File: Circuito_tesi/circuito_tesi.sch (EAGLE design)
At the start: 35 parts, among them IC3.3 317T, IC5 317T, U1 NRF52832, U2 BME688, U3 MICS-6814, U4 OPA2277PA, U5 OPA2277PA

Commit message: Aggiunti circuiti su board
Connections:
- net 3.3: no longer B1.GND, B1.GND@2
- net GND: now also B1.GND, B1.GND@2
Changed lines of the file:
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@@
 <net name="3.3" class="0">
-<segment>
-<pinref part="B1" gate="G$1" pin="GND"/>
-<wire x1="-129.54" y1="190.5" x2="-109.22" y2="190.5" width="0.1524" layer="91"/>
-<wire x1="-109.22" y1="190.5" x2="-109.22" y2="195.58" width="0.1524" layer="91"/>
-<pinref part="GND5" gate="1" pin="GND"/>
-<wire x1="-109.22" y1="195.58" x2="-104.14" y2="195.58" width="0.1524" layer="91"/>
-</segment>
-<segment>
-<pinref part="B1" gate="G$1" pin="GND@2"/>
-<wire x1="-162.56" y1="190.5" x2="-180.34" y2="190.5" width="0.1524" layer="91"/>
-<wire x1="-180.34" y1="190.5" x2="-180.34" y2="195.58" width="0.1524" layer="91"/>
-<pinref part="GND6" gate="1" pin="GND"/>
-<wire x1="-180.34" y1="195.58" x2="-187.96" y2="195.58" width="0.1524" layer="91"/>
-</segment>
 <segment>
 <wire x1="-228.6" y1="104.14" x2="-228.6" y2="119.38" width="0.1524" layer="91"/>
@@
 <pinref part="820OHM" gate="G$1" pin="2"/>
 <pinref part="U4" gate="A" pin="V+"/>
-<pinref part="U4" gate="A" pin="V+"/>
 <junction x="93.98" y="195.58"/>
 <pinref part="U5" gate="A" pin="V+"/>
@@
 <wire x1="127" y1="104.14" x2="127" y2="101.6" width="0.1524" layer="91"/>
 </segment>
+<segment>
+<pinref part="B1" gate="G$1" pin="GND@2"/>
+<wire x1="-162.56" y1="190.5" x2="-180.34" y2="190.5" width="0.1524" layer="91"/>
+<wire x1="-180.34" y1="190.5" x2="-180.34" y2="195.58" width="0.1524" layer="91"/>
+<pinref part="GND6" gate="1" pin="GND"/>
+<wire x1="-180.34" y1="195.58" x2="-187.96" y2="195.58" width="0.1524" layer="91"/>
+</segment>
+<segment>
+<pinref part="B1" gate="G$1" pin="GND"/>
+<wire x1="-129.54" y1="190.5" x2="-109.22" y2="190.5" width="0.1524" layer="91"/>
+<wire x1="-109.22" y1="190.5" x2="-109.22" y2="195.58" width="0.1524" layer="91"/>
+<pinref part="GND5" gate="1" pin="GND"/>
+<wire x1="-109.22" y1="195.58" x2="-104.14" y2="195.58" width="0.1524" layer="91"/>
+</segment>
 </net>
 <net name="N$2" class="0">
@@
 <pinref part="BT2" gate="G$1" pin="+"/>
 <wire x1="-109.22" y1="314.96" x2="-101.6" y2="314.96" width="0.1524" layer="91"/>
-</segment>
-</net>
-<net name="N$4" class="0">
-<segment>
-<pinref part="BT2" gate="G$1" pin="-"/>
-<pinref part="BT3" gate="G$1" pin="+"/>
-<wire x1="-86.36" y1="314.96" x2="-81.28" y2="314.96" width="0.1524" layer="91"/>
 </segment>
 </net>
@@
 </segment>
 </net>
+<net name="N$4" class="0">
+<segment>
+<pinref part="BT2" gate="G$1" pin="-"/>
+<pinref part="BT3" gate="G$1" pin="+"/>
+<wire x1="-86.36" y1="314.96" x2="-81.28" y2="314.96" width="0.1524" layer="91"/>
+</segment>
+</net>

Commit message: Aggiunte resistenze e condensatori smd
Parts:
- removed 10_MOHM, 10_MOHM1, 10_MOHM2, 130OHM, 27OHM, 300_OHM, 5_MOHM, 5_MOHM1, 5_MOHM2, 820OHM: 1614992-1, 1614992-1:1614992-1
- added R10: RMCF0603FT270R, Res_270OHM:RMCF0603FT270R
- added R11: RMCF0603FT130R, Res_130OHM:RMCF0603FT130R
- added R12: RMCF0603FT300R, Res_300OHM:RMCF0603FT300R
- added R3, R4, R5: RMCF0603FT10M0, Res_10MOHM_2:RMCF0603FT10M0
- added R6, R7, R8: RMCF0603FT5M10, Res_5.1MOHM:RMCF0603FT5M10
- added R9: RNCF0603DTE820R, Res_820OHM:RNCF0603DTE820R
- C3: value (none) -> 0.33µF; device capacitor-wima:C2,5-3 -> SparkFun-Capacitors:0.33UF/330NF-0805-50V-10%
- C4: value (none) -> 0.1uF; device capacitor-wima:C2,5-3 -> SparkFun-Capacitors:0.1UF-0603-25V-5%
- C5: value 0.33µF -> GRM033R60J103KA01D; device SparkFun-Capacitors:0.33UF/330NF-0805-50V-10% -> Condens_10nF:GRM033R60J103KA01D
- C6: value 0.1uF -> GRM033R60J103KA01D; device SparkFun-Capacitors:0.1UF-0603-25V-5% -> Condens_10nF:GRM033R60J103KA01D
- C7: value (none) -> GRM033R60J103KA01D; device capacitor-wima:C2,5-3 -> Condens_10nF:GRM033R60J103KA01D
- R1, R2: value 10k -> RNCF0603BTE10K0; device SparkFun-Resistors:10KOHM-HORIZ-1/6W-5% -> Res_10KOHM:RNCF0603BTE10K0
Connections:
- removed net N$18: 10_MOHM1.2, 5_MOHM1.1, C4.1, U1.P0.03/AIN1
- new net N$15: C6.2, R4.2, R7.1, U1.P0.03/AIN1
- net 5V: now also C4.1, R10.2, R11.2, R9.2; no longer 130OHM.2, 27OHM.2, 820OHM.2, C6.1
- net GND: now also C5.1, C6.1, C7.1, R12.1, R3.1, R4.1, R5.1; no longer 10_MOHM.1, 10_MOHM1.1, 10_MOHM2.1, 300_OHM.1, C5.2, C6.2, C7.2
- net N$11: now also R9.1; no longer 820OHM.1
- net N$12: now also R10.1; no longer 27OHM.1
- net N$13: now also R11.1; no longer 130OHM.1
- net N$16: now also C7.2, R5.2, R8.1; no longer 10_MOHM2.2, 5_MOHM2.1, C3.1
- net N$17: now also C5.2, R3.2, R6.1; no longer 10_MOHM.2, 5_MOHM.1, C7.1
- net N$22: now also R6.2; no longer 5_MOHM.2
- net N$7: now also R7.2; no longer 5_MOHM1.2
- net N$8: now also R8.2; no longer 5_MOHM2.2
- net N$9: now also R12.2; no longer 300_OHM.2
- net VDD: now also C3.1; no longer C5.1
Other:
- note removed: "ATTENZIONE: resistenze mics non corrispondono ai valori richiesti, valore scritto in numero"
- moved on the sheet: C3, C4, C5, C6, C7, R1, R2

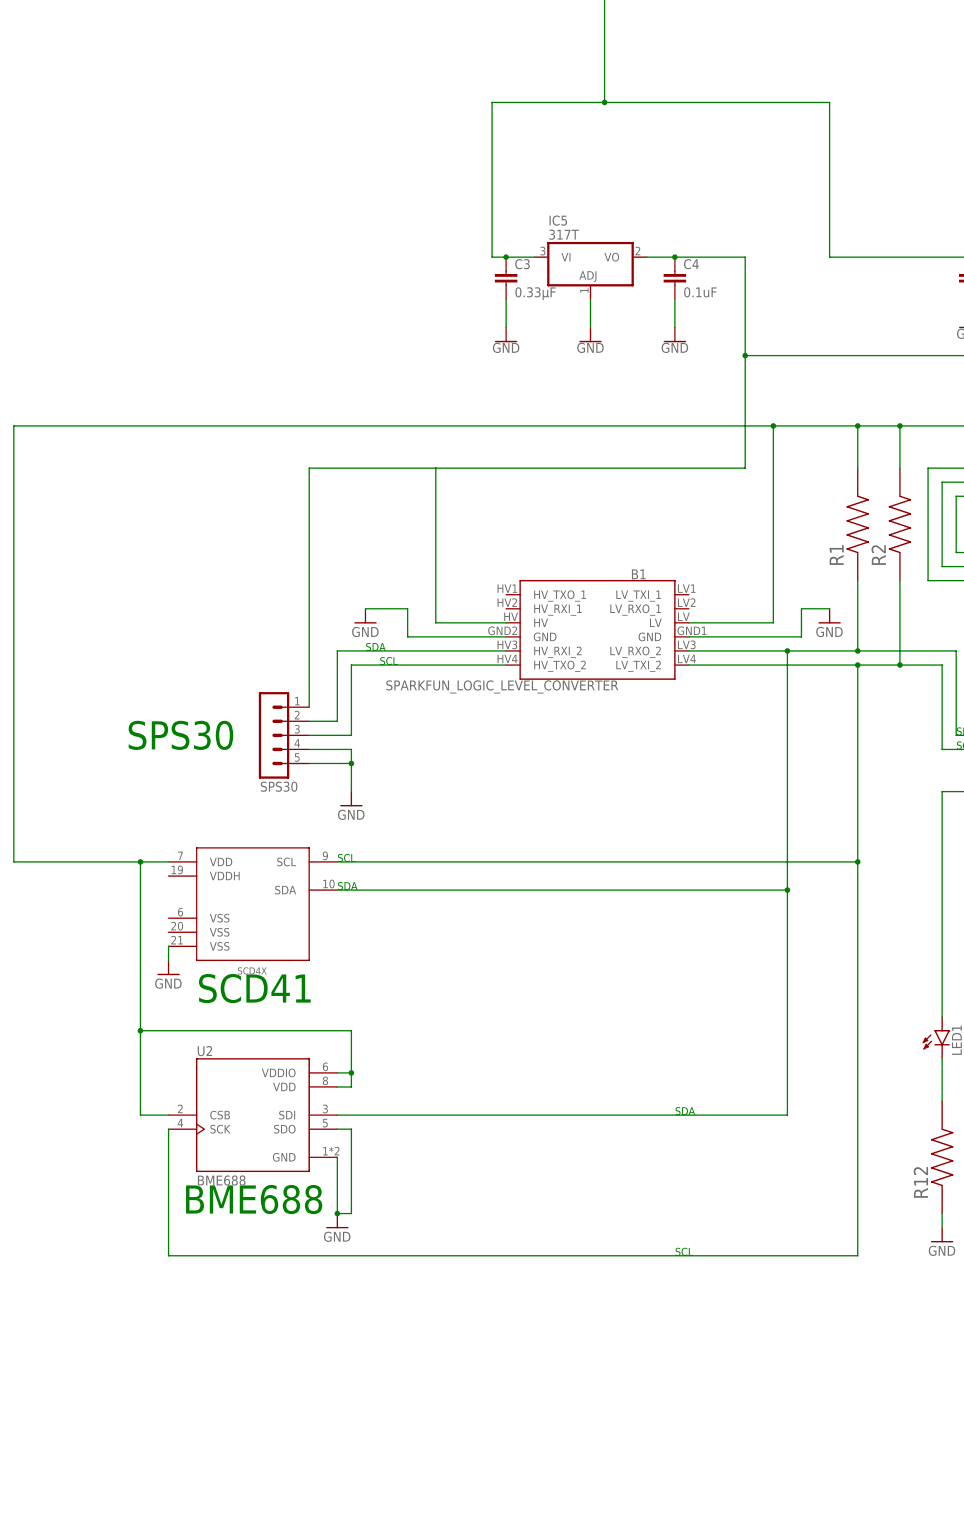
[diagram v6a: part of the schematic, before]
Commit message: Aggiunto BME280 e SGP30
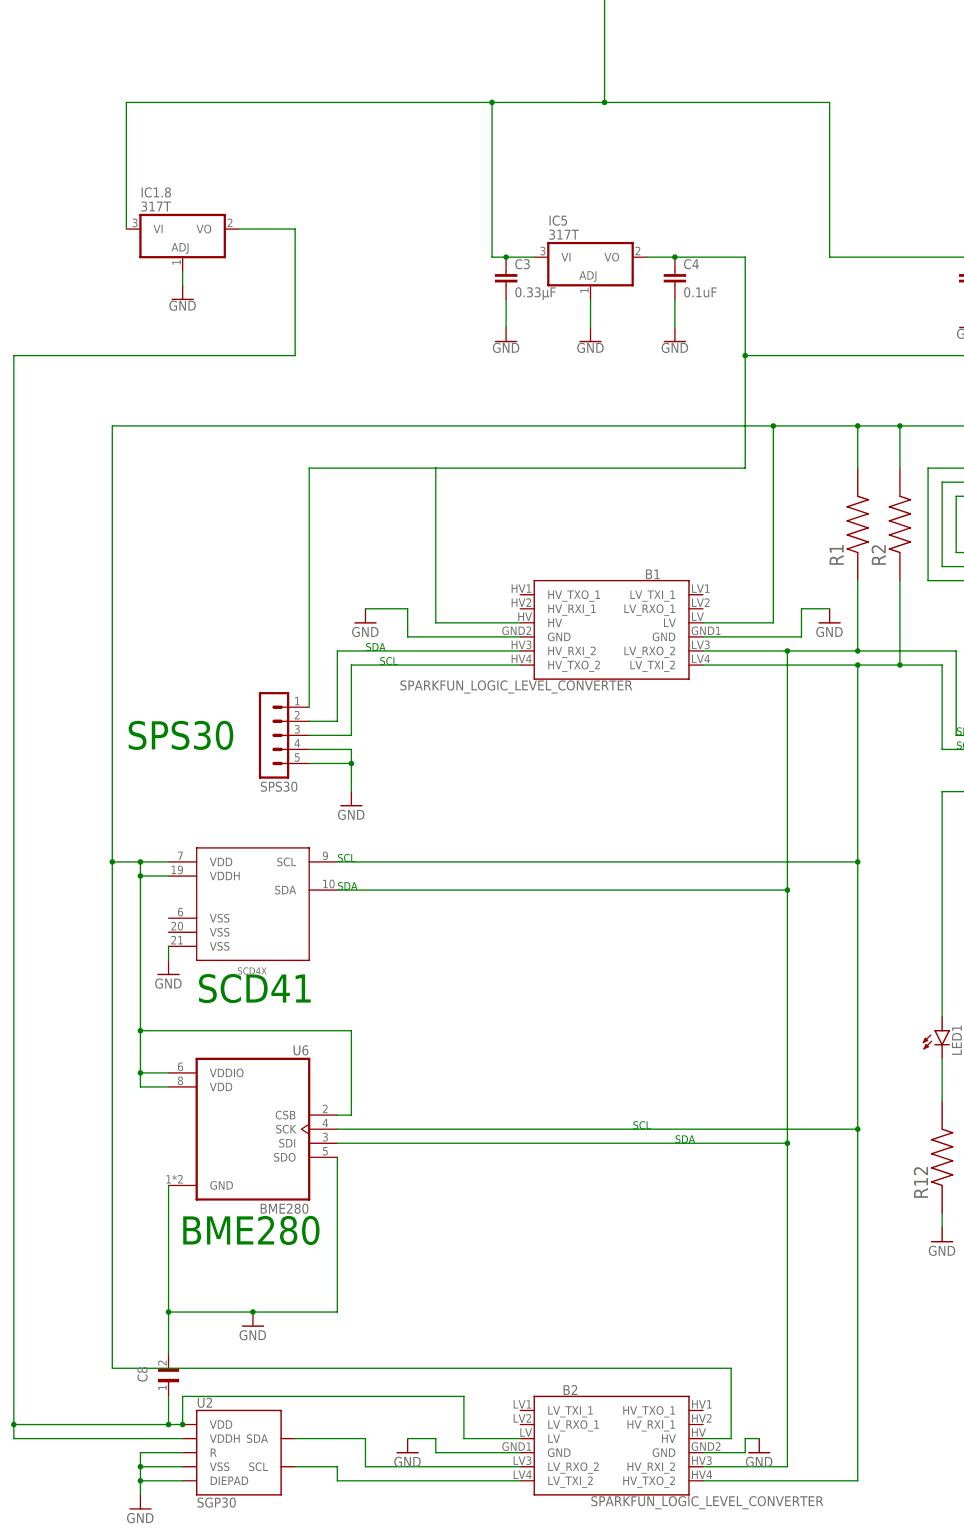
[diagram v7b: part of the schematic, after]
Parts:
- added B2: SPARKFUN_LOGIC_LEVEL_CONVERTER, SparkFun-Boards:SPARKFUN_LOGIC_LEVEL_CONVERTER
- added C8: GRM033C80J104KE15D, Condens_100nF:GRM033C80J104KE15D
- added IC1.8: 317T, linear:317T
- added U6: BME280, BME280:BME280
- U2: value BME688 -> SGP30; device BME688:BME688 -> SGP30:SGP30
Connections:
- new net 1.8V: B2.LV, C8.1, IC1.8.VO, U2.VDD, U2.VDDH
- new net N$20: B2.LV_RXO_2, U2.SDA
- new net N$23: B2.LV_TXI_2, U2.SCL
- net 3.3: now also B2.HV, SCD4X.VDDH, U6.CSB, U6.VDD, U6.VDDIO; no longer U2.CSB, U2.VDD, U2.VDDIO
- net GND: now also B2.GND, B2.GND@2, C8.2, IC1.8.ADJ, U2.DIEPAD, U2.R, U2.VSS, U6.GND, U6.SDO; no longer U2.GND, U2.SDO
- net SCL: now also B2.HV_TXO_2, U6.SCK; no longer U2.SCK
- net SDA: now also B2.HV_RXI_2, U6.SDI; no longer U2.SDI
- net VDD: now also IC1.8.VI
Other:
- note added: "BME280"
- note removed: "BME688"
- moved on the sheet: B1

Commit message: Aggiunto ACCELEROMETRO
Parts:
- removed C7: GRM033R60J103KA01D, Condens_10nF:GRM033R60J103KA01D
- removed R10: RMCF0603FT270R, Res_270OHM:RMCF0603FT270R
- removed R8: RMCF0603FT5M10, Res_5.1MOHM:RMCF0603FT5M10
- removed U5: OPA2277PA, OPA2277PA:OPA2277PA
- added Q1: BSS138, BSS138:BSS138
- added U7: LIS3DH, LIS3DH:LIS3DH
- R5: value RMCF0603FT10M0 -> RNCF0603BTE10K0; device Res_10MOHM_2:RMCF0603FT10M0 -> Res_10KOHM:RNCF0603BTE10K0
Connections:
- removed net N$12: R10.1, U3.RH1_NH3
- removed net N$14: U3.RS1_NH3, U5.+IN_A
- removed net N$16: C7.2, R5.2, R8.1, U1.P0.04/AIN2
- net 1.8V: now also U7.CS, U7.VDD, U7.VDD_IO
- net 5V: no longer R10.2, U5.V+
- net GND: now also U7.GND, U7.GND1, U7.RES, U7.SDO/SA0; no longer C7.1, R5.1, U3.RS2_NH3, U5.V-
- net N$11: no longer U3.RH2_NH3
- net N$17: now also R6.2; no longer R6.1
- net N$20: now also U7.SDA/SDI/SDO
- net N$22: now also R6.1; no longer R6.2
- net N$23: now also U7.SCL/SPC
- net N$8: now also R5.2; no longer R8.2, U5.-IN_A, U5.OUT_A
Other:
- note added: "LIS3DH"
- note added: "SGP30"
- moved on the sheet: C5, C6, R11, R3, R4, R5, R6, R7, R9, U3, U4
